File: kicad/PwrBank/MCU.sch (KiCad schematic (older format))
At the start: 8 parts, among them U2 ESP32-DEVKITC-32D

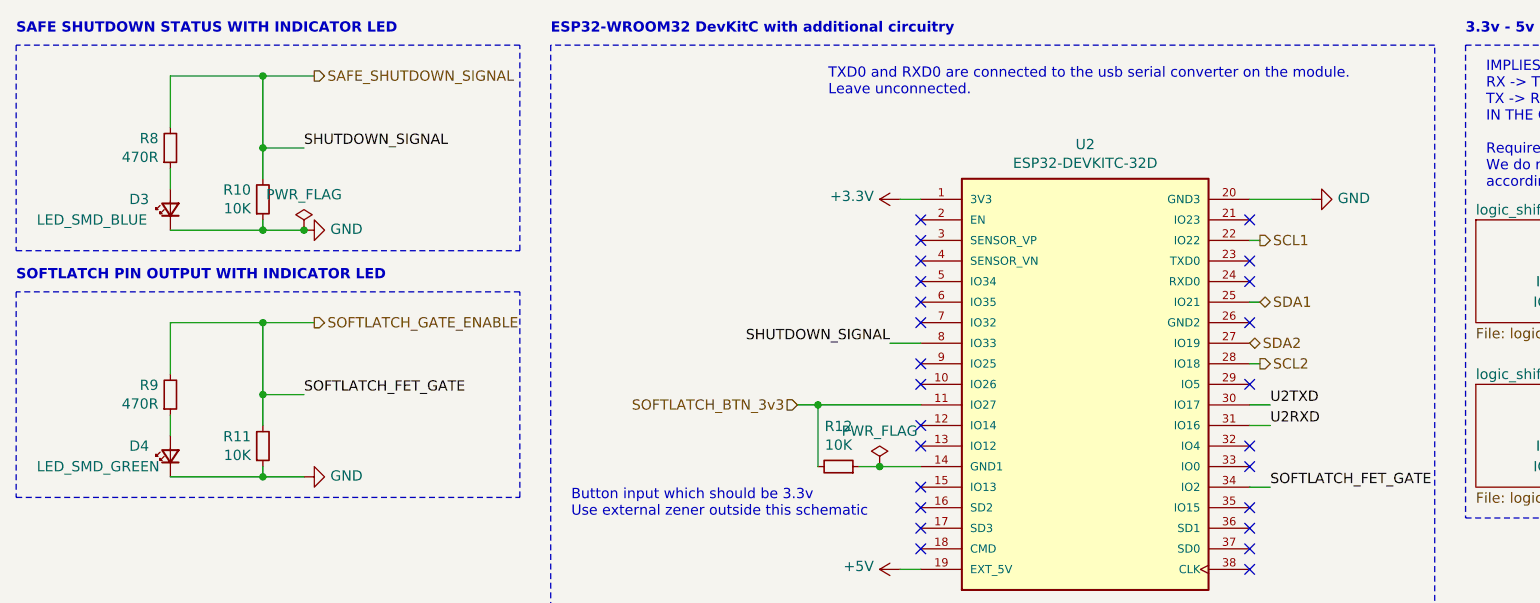
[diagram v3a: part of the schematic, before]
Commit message: Work on schematic+implement capacitive feature using TOUCH0
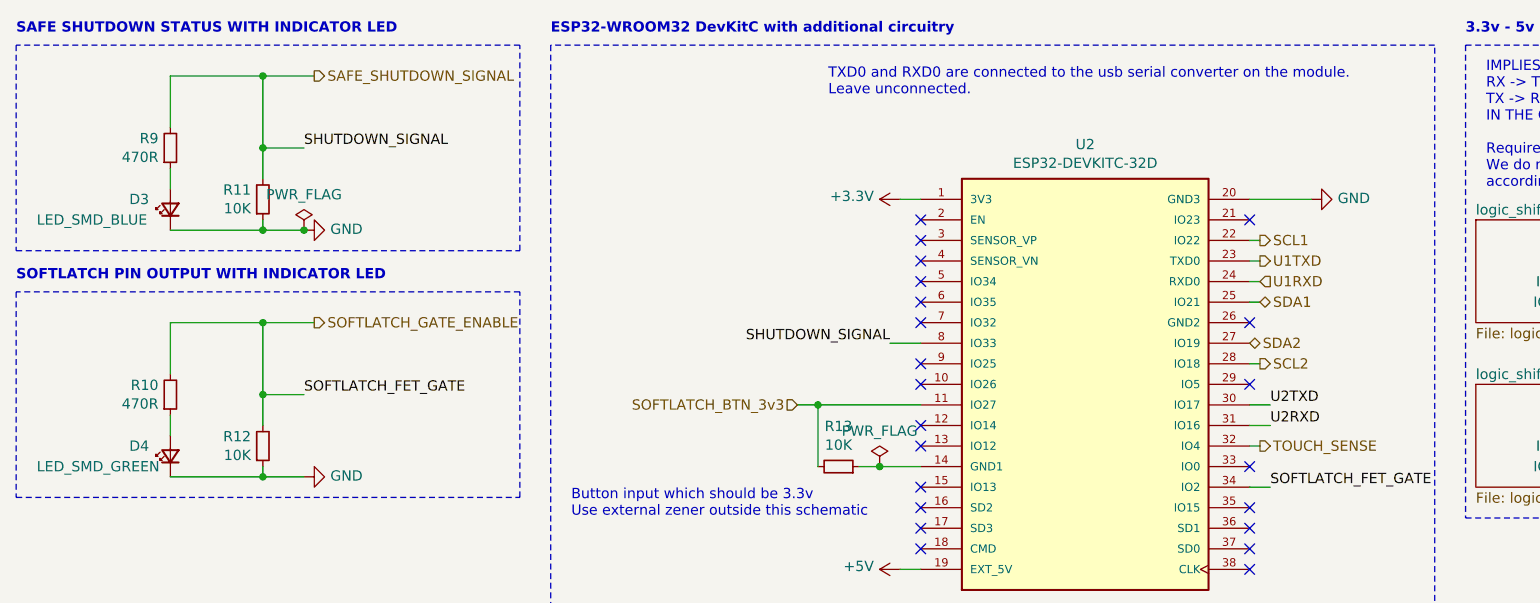
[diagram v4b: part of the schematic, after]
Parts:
- renumbered R9 to R10, R10 to R11, R11 to R12, R12 to R13, R8 to R9
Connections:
- net U1TXD: now reaches U2.23 (TXD0)
- net U1RXD: now reaches U2.24 (RXD0)
- net TOUCH_SENSE: now reaches U2.32 (IO4)
- no-connect marks 25 -> 22
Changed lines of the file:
@@
 $Descr A4 11693 8268
 encoding utf-8
-Sheet 6 9
+Sheet 5 9
 Title "ESP32_Devkit_Addons"
 Date "2021-07-17"
@@
 BMS_TX
 $Comp
-L Device:R_Small R12
+L Device:R_Small R13
 U 1 1 60F3049F
 P 4850 3300
-F 0 "R12" V 5046 3300 50  0000 C CNN
+F 0 "R13" V 5046 3300 50  0000 C CNN
 F 1 "10K" V 4955 3300 50  0000 C CNN
 F 2 "Resistor_SMD:R_0805_2012Metric_Pad1.20x1.40mm_HandSolder" H 4850 3300 50  0001 C CNN
@@
 Wire Wire Line
 	7150 2000 6850 2000
-NoConn ~ 6850 2300
-NoConn ~ 6850 2400
 Text Notes 4800 1500 0    50   ~ 0
 TXD0 and RXD0 are connected to the usb serial converter on the module.\nLeave unconnected.
@@
 	2300 1400 2050 1400
 $Comp
-L Device:R_Small R10
+L Device:R_Small R11
 U 1 1 60F71BF4
 P 2050 2000
-F 0 "R10" H 1992 1954 50  0000 R CNN
+F 0 "R11" H 1992 1954 50  0000 R CNN
 F 1 "10K" H 1992 2045 50  0000 R CNN
 F 2 "Resistor_SMD:R_0805_2012Metric_Pad1.20x1.40mm_HandSolder" H 2050 2000 50  0001 C CNN
@@
 	1600 2150 2050 2150
 $Comp
-L Device:R_Small R8
+L Device:R_Small R9
 U 1 1 60F80C8C
 P 1600 1750
-F 0 "R8" H 1542 1704 50  0000 R CNN
+F 0 "R9" H 1542 1704 50  0000 R CNN
 F 1 "470R" H 1542 1795 50  0000 R CNN
 F 2 "Resistor_SMD:R_0805_2012Metric_Pad1.20x1.40mm_HandSolder" H 1600 1750 50  0001 C CNN
@@
 	2300 2600 2050 2600
 $Comp
-L Device:R_Small R11
+L Device:R_Small R12
 U 1 1 60F351CF
 P 2050 3200
-F 0 "R11" H 1992 3154 50  0000 R CNN
+F 0 "R12" H 1992 3154 50  0000 R CNN
 F 1 "10K" H 1992 3245 50  0000 R CNN
 F 2 "Resistor_SMD:R_0805_2012Metric_Pad1.20x1.40mm_HandSolder" H 2050 3200 50  0001 C CNN
@@
 	1600 3350 2050 3350
 $Comp
-L Device:R_Small R9
+L Device:R_Small R10
 U 1 1 60F351DA
 P 1600 2950
-F 0 "R9" H 1542 2904 50  0000 R CNN
+F 0 "R10" H 1542 2904 50  0000 R CNN
 F 1 "470R" H 1542 2995 50  0000 R CNN
 F 2 "Resistor_SMD:R_0805_2012Metric_Pad1.20x1.40mm_HandSolder" H 1600 2950 50  0001 C CNN
@@
 NoConn ~ 6850 3500
 NoConn ~ 6850 3300
-NoConn ~ 6850 3200
 NoConn ~ 6850 2900
 NoConn ~ 6850 2600
@@
 	5150 3800 5250 3800
 $Comp
-L power:GND #PWR029
+L power:GND #PWR031
 U 1 1 61034275
 P 7150 2000
-F 0 "#PWR029" H 7150 1750 50  0001 C CNN
+F 0 "#PWR031" H 7150 1750 50  0001 C CNN
 F 1 "GND" V 7155 1872 50  0000 R CNN
 F 2 "" H 7150 2000 50  0001 C CNN
@@
 $EndComp
 $Comp
-L power:GND #PWR025
+L power:GND #PWR027
 U 1 1 61035069
 P 2250 2150
-F 0 "#PWR025" H 2250 1900 50  0001 C CNN
+F 0 "#PWR027" H 2250 1900 50  0001 C CNN
 F 1 "GND" V 2255 2022 50  0000 R CNN
 F 2 "" H 2250 2150 50  0001 C CNN
@@
 $EndComp
 $Comp
-L power:GND #PWR026
+L power:GND #PWR028
 U 1 1 61035606
 P 2250 3350
-F 0 "#PWR026" H 2250 3100 50  0001 C CNN
+F 0 "#PWR028" H 2250 3100 50  0001 C CNN
 F 1 "GND" V 2255 3222 50  0000 R CNN
 F 2 "" H 2250 3350 50  0001 C CNN
@@
 $EndComp
 $Comp
-L power:+3.3V #PWR027
+L power:+3.3V #PWR029
 U 1 1 61037CC9
 P 5150 2000
-F 0 "#PWR027" H 5150 1850 50  0001 C CNN
+F 0 "#PWR029" H 5150 1850 50  0001 C CNN
 F 1 "+3.3V" V 5165 2128 50  0000 L CNN
 F 2 "" H 5150 2000 50  0001 C CNN
@@
 $EndComp
 $Comp
-L power:+5V #PWR028
+L power:+5V #PWR030
 U 1 1 61038914
 P 5150 3800
-F 0 "#PWR028" H 5150 3650 50  0001 C CNN
+F 0 "#PWR030" H 5150 3650 50  0001 C CNN
 F 1 "+5V" V 5165 3928 50  0000 L CNN
 F 2 "" H 5150 3800 50  0001 C CNN
@@
 $EndSheet
 $Comp
-L power:+5V #PWR030
+L power:+5V #PWR032
 U 1 1 61039E33
 P 8600 2200
-F 0 "#PWR030" H 8600 2050 50  0001 C CNN
+F 0 "#PWR032" H 8600 2050 50  0001 C CNN
 F 1 "+5V" V 8615 2328 50  0000 L CNN
 F 2 "" H 8600 2200 50  0001 C CNN
@@
 $EndComp
 $Comp
-L power:+3.3V #PWR031
+L power:+3.3V #PWR033
 U 1 1 6103A5D9
 P 8600 2300
-F 0 "#PWR031" H 8600 2150 50  0001 C CNN
+F 0 "#PWR033" H 8600 2150 50  0001 C CNN
 F 1 "+3.3V" V 8615 2428 50  0000 L CNN
 F 2 "" H 8600 2300 50  0001 C CNN
@@
 $EndComp
 $Comp
-L power:+5V #PWR032
+L power:+5V #PWR034
 U 1 1 6103DF7E
 P 8600 3000
-F 0 "#PWR032" H 8600 2850 50  0001 C CNN
+F 0 "#PWR034" H 8600 2850 50  0001 C CNN
 F 1 "+5V" V 8615 3128 50  0000 L CNN
 F 2 "" H 8600 3000 50  0001 C CNN
@@
 $EndComp
 $Comp
-L power:+3.3V #PWR033
+L power:+3.3V #PWR035
 U 1 1 6103E675
 P 8600 3100
-F 0 "#PWR033" H 8600 2950 50  0001 C CNN
+F 0 "#PWR035" H 8600 2950 50  0001 C CNN
 F 1 "+3.3V" V 8615 3228 50  0000 L CNN
 F 2 "" H 8600 3100 50  0001 C CNN
@@
 Text HLabel 6850 2700 2    50   BiDi ~ 0
 SDA2
+Text HLabel 6900 2300 2    50   Output ~ 0
+U1TXD
+Text HLabel 6900 2400 2    50   Input ~ 0
+U1RXD
+Wire Wire Line
+	6850 2300 6900 2300
+Wire Wire Line
+	6850 2400 6900 2400
+Text HLabel 6900 3200 2    50   Output ~ 0
+TOUCH_SENSE
+Wire Wire Line
+	6900 3200 6850 3200
 $EndSCHEMATC
